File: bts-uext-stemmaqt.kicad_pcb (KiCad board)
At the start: 2 copper layers, 25.4 x 15.2 mm, 2 parts, among them J2 Conn_01x04, J3 UEXT_Slave

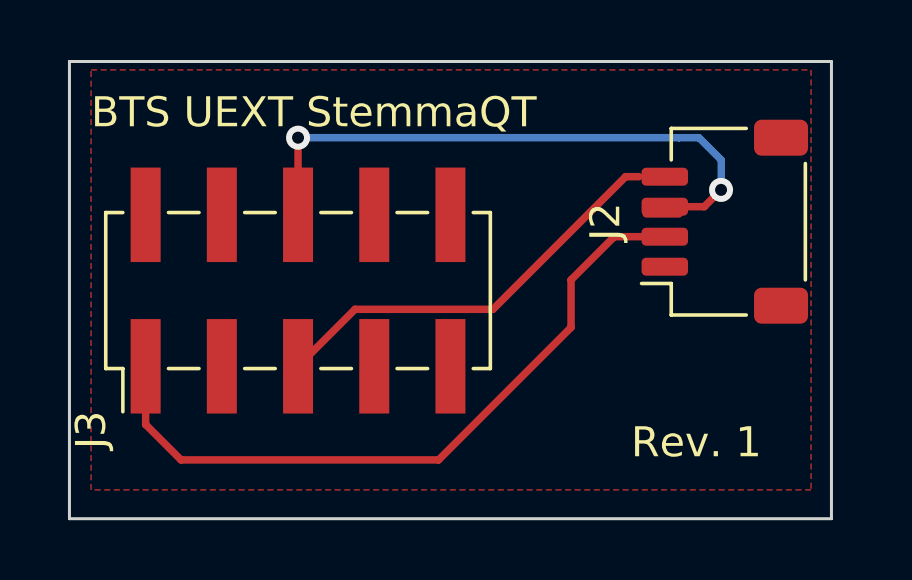
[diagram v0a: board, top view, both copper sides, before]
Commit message: Rev2: Switch 2x5 to through hole.
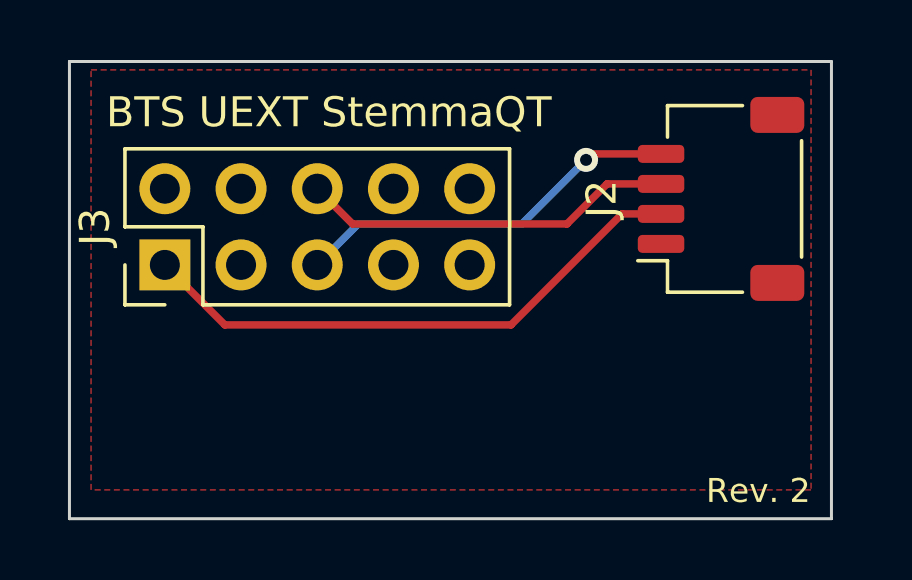
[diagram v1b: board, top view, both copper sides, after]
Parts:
- J2: value Conn_01x04 -> Stemma QT
- J3: footprint Connector_PinHeader_2.54mm:PinHeader_2x05_P2.54mm_Vertical_SMD -> Connector_PinHeader_2.54mm:PinHeader_2x05_P2.54mm_Vertical
- moved J3 4.52 mm to (84.5, 52.5)
- moved J2 0.77 mm to (103.0, 50.3)
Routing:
- net SDA: track 21.2 -> 12.5 mm, vias 2 -> 0
- net +3V3: track 23.7 -> 18.9 mm
- net SCL: track 14.0 -> 13.0 mm, vias 0 -> 1
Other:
- board text added: "Rev. 2"
- board text removed: "Rev. 1"
